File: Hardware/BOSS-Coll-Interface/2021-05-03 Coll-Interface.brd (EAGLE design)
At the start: 88.9 x 38.1 mm, 5 parts, among them J1 Amphenol 75869-330LF, J2 TE_1-2834016-2, X1 Amphenol L77SDC37S1ACH4RC309

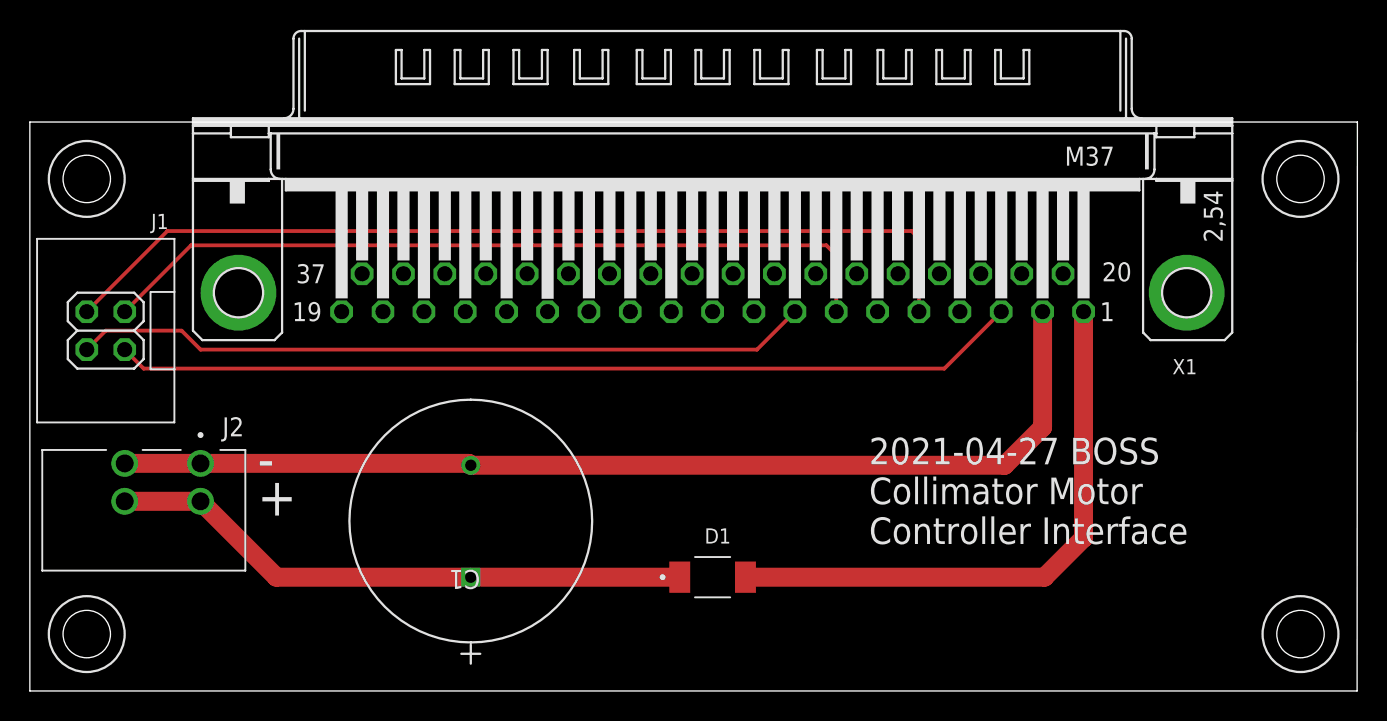
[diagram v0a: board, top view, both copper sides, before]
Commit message: Made a 2021-05-03 copy, to manufacture (2021-04-27 needed a change)
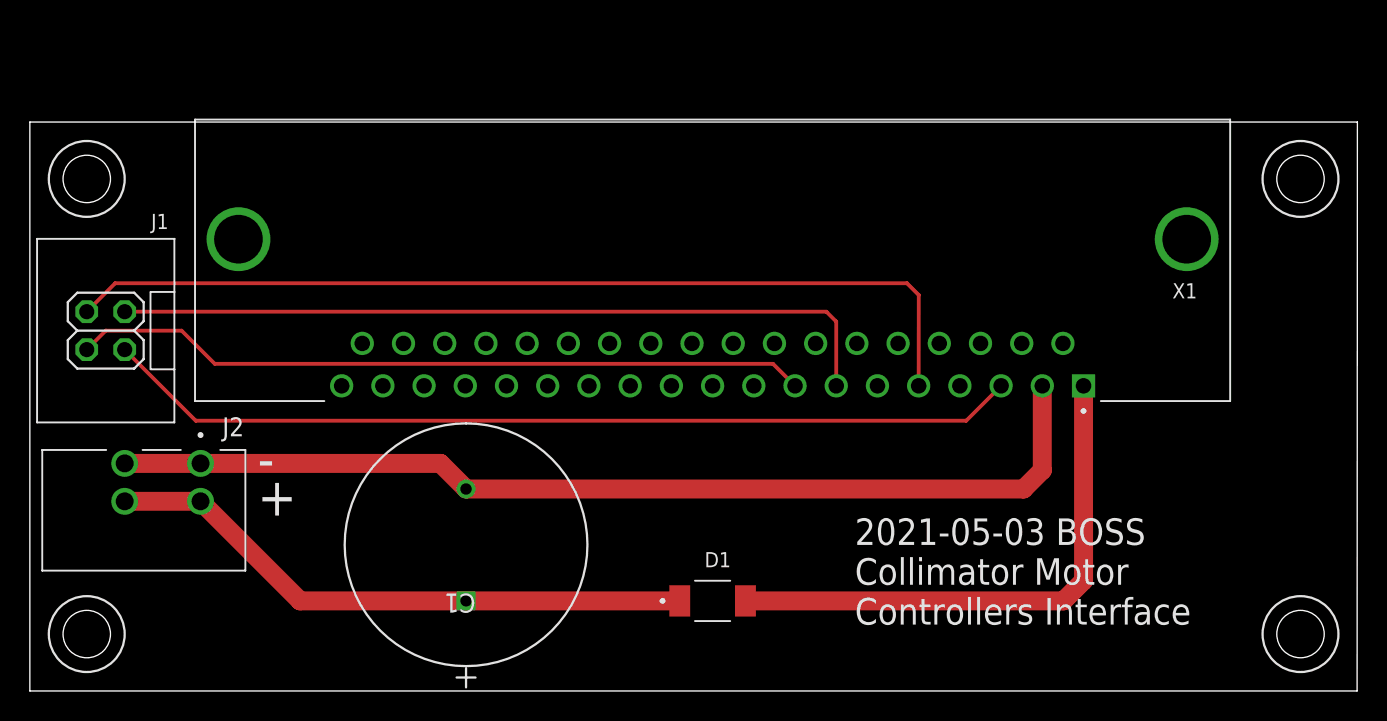
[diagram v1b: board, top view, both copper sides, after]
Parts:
- X1: value Amphenol L77SDC37S1ACH4RC309 -> TE 5747835-4; device AUmlib:M37HP -> AUmlib:TE_5747835-4
- moved X1 5.08 mm to (45.7, 31.8)
- moved C1 1.62 mm to (29.2, 6.03)
- moved D1 1.59 mm to (45.7, 6.03)
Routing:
- net +24V-FROM-SPECMECH: track 38.9 -> 36.3 mm
- net GND-ROBOCLAW: track 70.3 -> 68.3 mm
- net ROBO-TX: track 53.5 -> 52.2 mm
- net ROBO-RX: track 60.8 -> 61.6 mm
- net +24V-TO-ROBOCLAW: track 39.3 -> 39.9 mm
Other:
- board text added: "2021-05-03 BOSS Collimator Motor Controllers Interface"
- board text removed: "2021-04-27 BOSS Collimator Motor Controller Interface"
